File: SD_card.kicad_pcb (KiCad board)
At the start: 2 copper layers, 9 parts, among them J1 Micro_SD_Card, J2 Conn_01x08

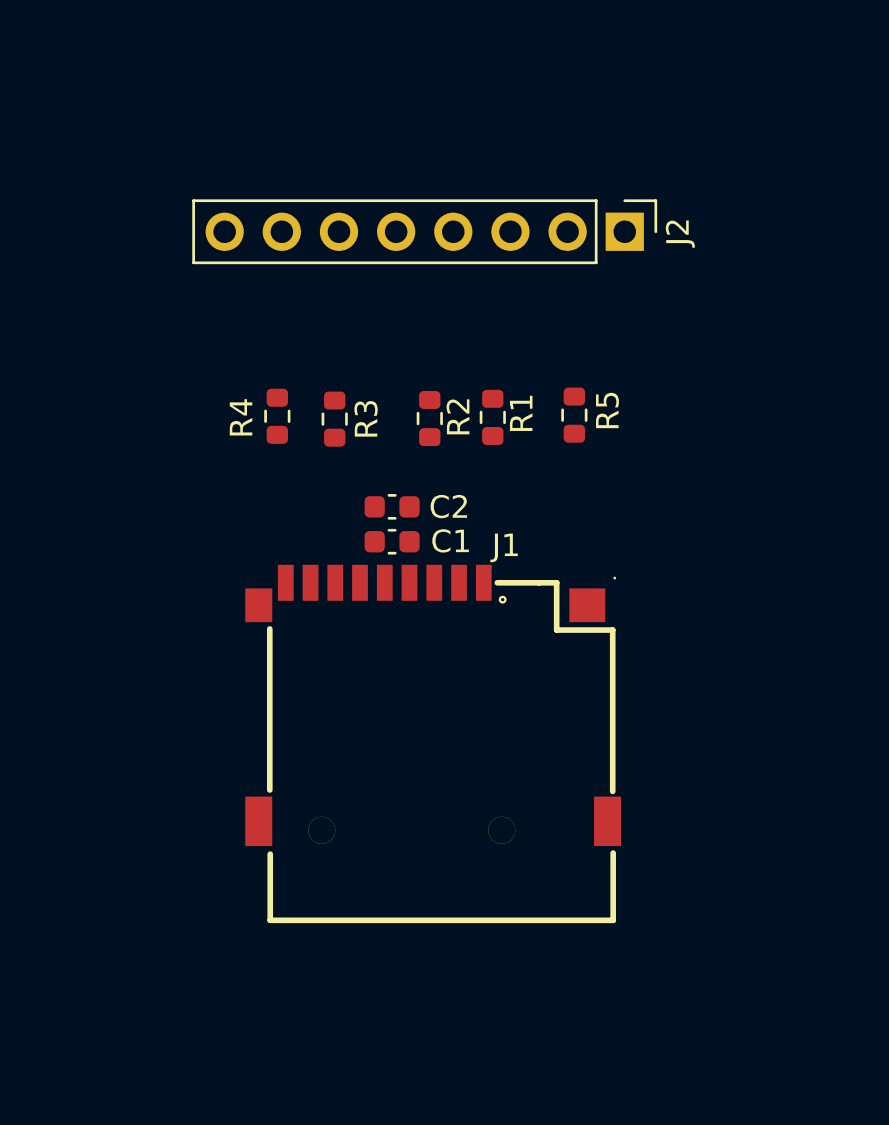
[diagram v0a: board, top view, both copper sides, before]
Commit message: Complete PCB layout, DRC clean
Routed all signals on F.Cu, GND pours on both layers with
stitching vias. Fixed imported connector footprint (courtyard,
NPTH holes, shell-tab naming). Added silkscreen labeling.
Ready for fab output generation.
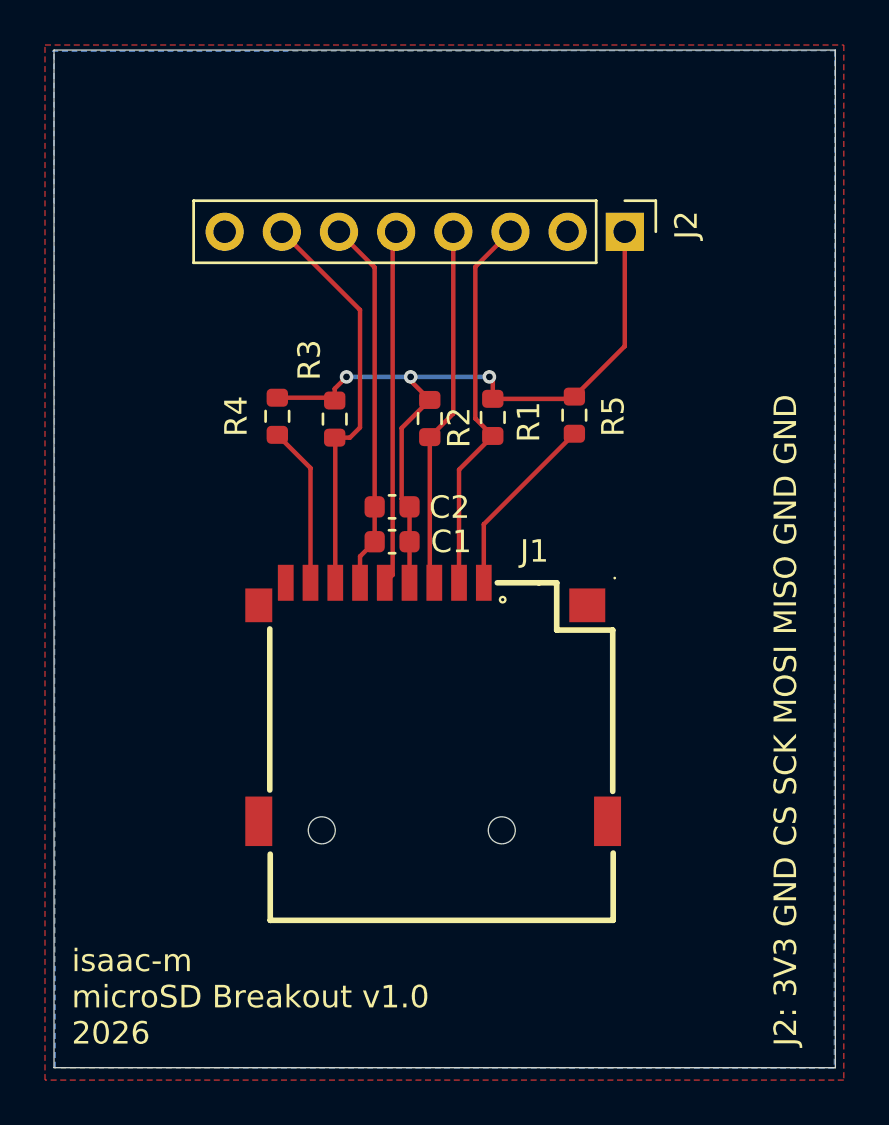
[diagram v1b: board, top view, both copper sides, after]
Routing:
- net +3V3: track 0.00 -> 33.6 mm, vias 0 -> 3
- net /MISO: track 0.00 -> 17.9 mm
- net /CS: track 0.00 -> 17.4 mm
- net GND: track 0.00 -> 16.5 mm
- net /MOSI: track 0.00 -> 16.1 mm
- net /SCK: track 0.00 -> 15.8 mm
- net Net-(J1-DAT2): track 0.00 -> 8.29 mm
- net Net-(J1-DAT1): track 0.00 -> 7.19 mm
- added copper zone on B.Cu, net GND
- added copper zone on F.Cu, net GND
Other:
- board outline added: 34.7 x 45.2 mm
- board text added: "J2: 3V3 GND CS SCK MOSI MISO GND GND"
- board text added: "isaac-m microSD Breakout v1.0 2026"
